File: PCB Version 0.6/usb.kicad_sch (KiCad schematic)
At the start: 5 parts, among them J1 USB_C_Receptacle_USB2.0_16P, J2 Conn_01x04_MountingPin, U8 WE-TVS-824015043

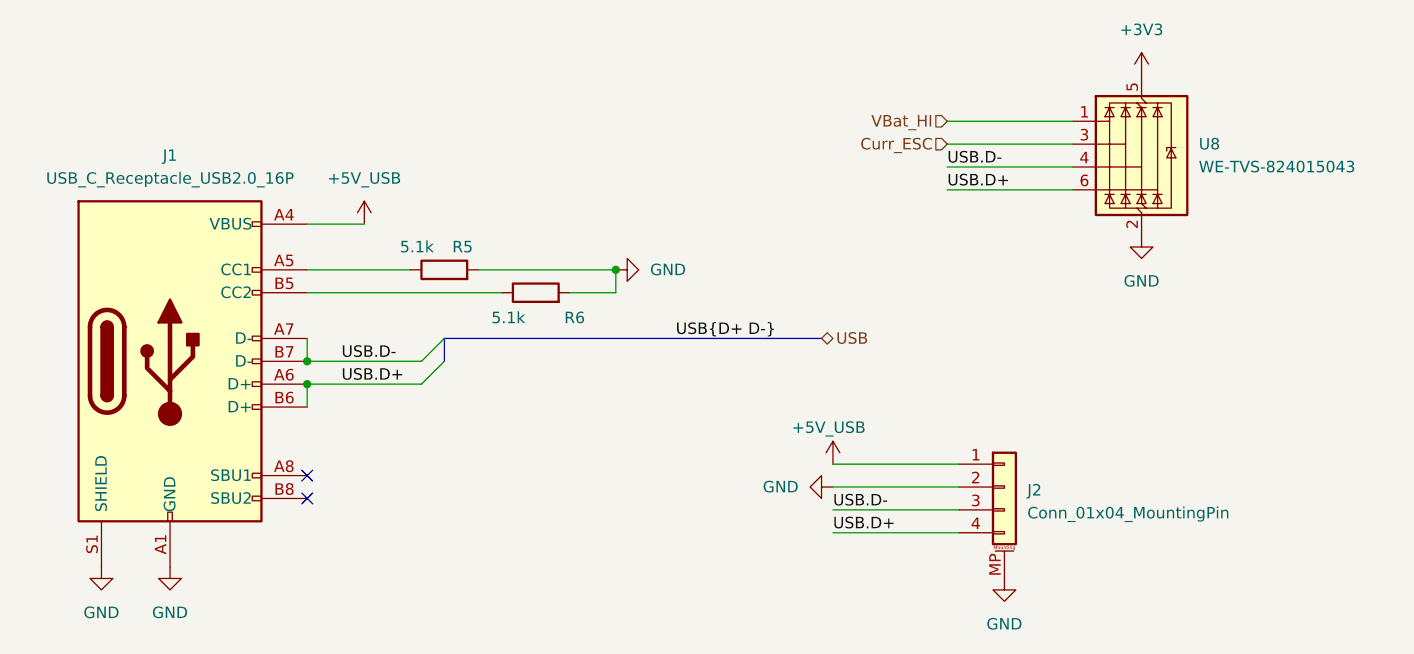
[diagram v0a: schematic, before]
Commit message: replace USB JST with pads and remove USB TVS
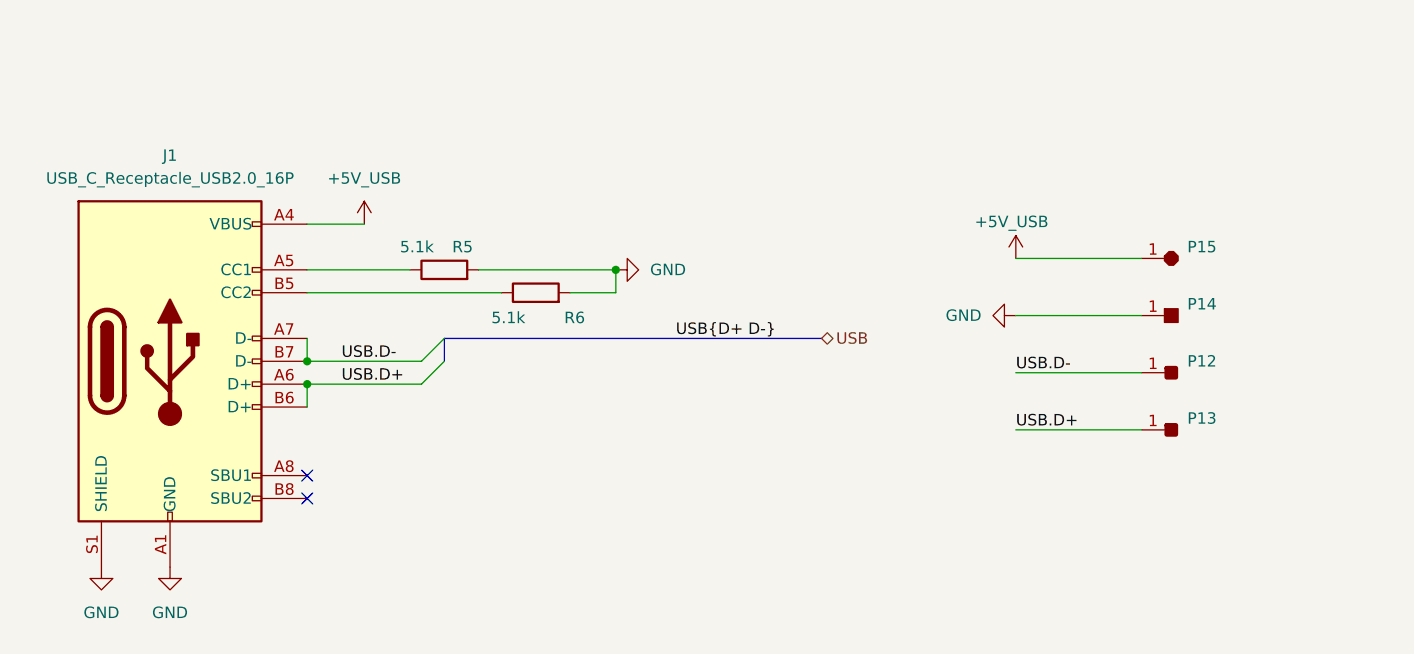
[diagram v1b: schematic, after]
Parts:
- removed J2: Conn_01x04_MountingPin, Connector_JST:JST_SH_SM04B-SRSS-TB_1x04-1MP_P1.00mm_Horizontal, symbol Connector_Generic_MountingPin:Conn_01x04_MountingPin
- removed U8: WE-TVS-824015043, Package_TO_SOT_SMD:SOT-23-6, symbol Power_Protection:WE-TVS-824015043
- added P12, P13: ~, Kolibri custom:Solder_Pad_rounded, symbol Kolibri custom:Solder_Pad_rounded
- added P14: ~, Kolibri custom:Solder_Pad_rect, symbol Kolibri custom:Solder_Pad_rect
- added P15: ~, Kolibri custom:Solder_Pad_octa, symbol Kolibri custom:Solder_Pad_octa
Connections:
- net +5V_USB: now also P15.1
- net GND: now also P14.1
- net USB.D+: now also P13.1
- net USB.D-: now also P12.1
